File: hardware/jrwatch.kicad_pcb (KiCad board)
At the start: 4 copper layers, 36 x 36 mm, 47 parts, among them J1 TYPE-C-31-M-12, J2 FH12A-10S-0.5SH, J3 SM02B-SRSS-TB, J4 TC2030-IDC-NL, SW1 PWR/SHIP, SW2 USER, U1 MDBT50Q-1MV2, U2 nPM1300-QEAA-R7, U3 BMI270, U4 USBLC6-2SC6, Y1 32.768kHz

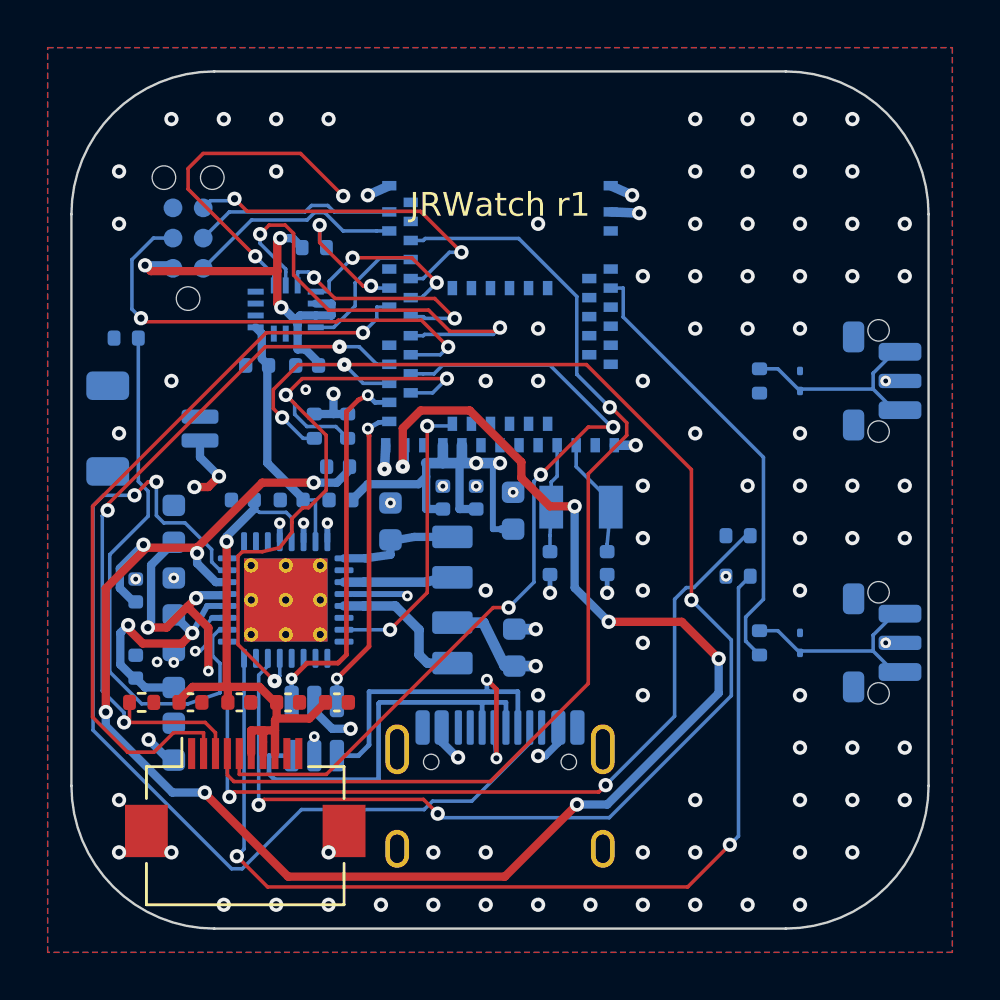
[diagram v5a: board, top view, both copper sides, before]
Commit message: WIP: land D-025 display connector rework (routing incomplete)
Scripted landing of D-025 via hardware/scripts/land_d025.py: J2 moved to
(100, 111.8) with tail-centered pads and mirrored pinout per Sharp fig 8-1,
USB CONN highways moved north, DM_CONN crossover rerouted through new vias,
CC1/CC2 landed on J1.A5/B5. Every coordinate hand clearance-checked
(0.13 mm copper, 0.25 mm hole-to-copper, 0.5 mm hole-to-hole).

State at this commit: DRC 32 errors / 20 unconnected (drc-links.json,
2026-07-03 12:57) — interactive routing cleanup still required before the
fab order gate.
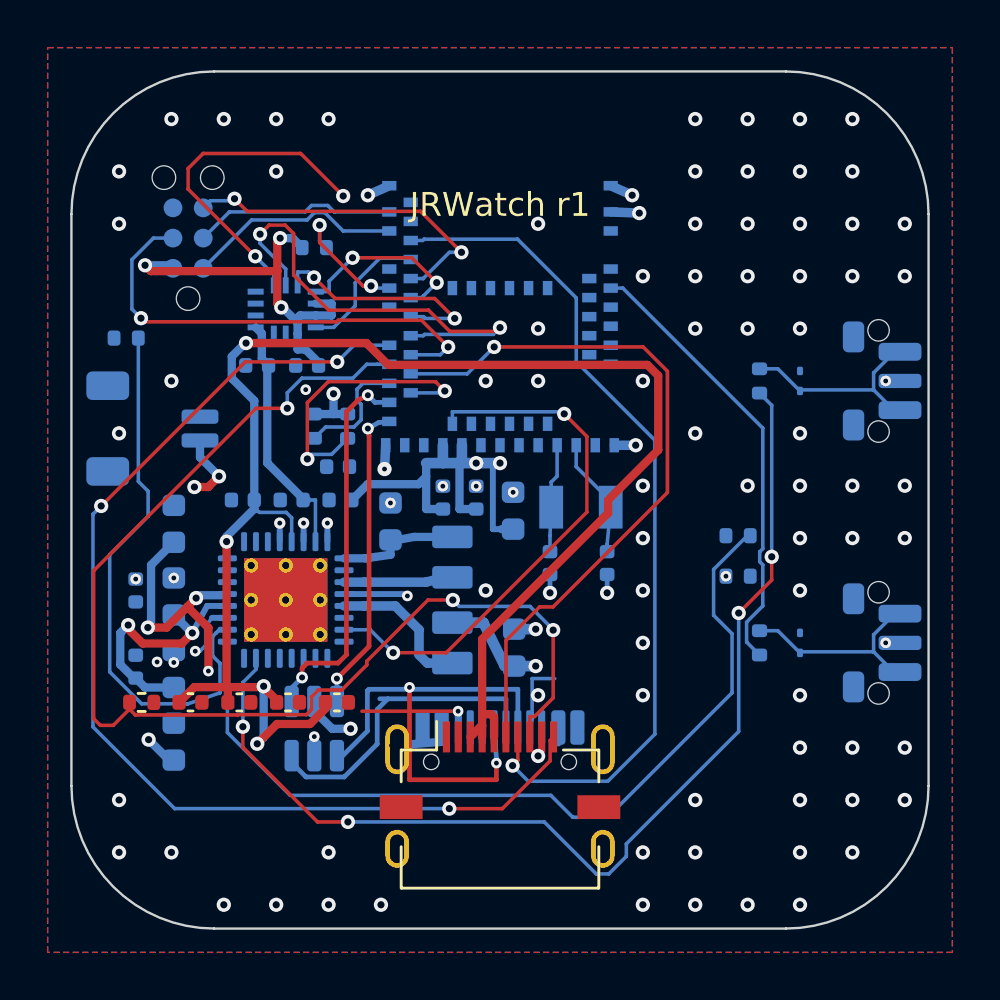
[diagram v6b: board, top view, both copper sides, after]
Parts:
- moved J2 10.7 mm to (100.0, 111.8)
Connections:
- J2 pad 1: DISP_SCK -> GND
- J2 pad 10: GND -> DISP_SCK
- J2 pad 2: DISP_MOSI -> GND
- J2 pad 3: DISP_CS -> VDD_DISP
- J2 pad 4: EXTCOMIN -> VDD_DISP
- J2 pad 5: DISP_ON -> VDD_DISP
- J2 pad 6: VDD_DISP -> DISP_ON
- J2 pad 7: VDD_DISP -> EXTCOMIN
- J2 pad 8: VDD_DISP -> DISP_CS
- J2 pad 9: GND -> DISP_MOSI
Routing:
- net VBUS_OUT: track 79.6 -> 0.00 mm, vias 10 -> 0
- net I2C_SCL: track 64.0 -> 5.10 mm, vias 5 -> 0
- net DISP_SCK: track 0.00 -> 46.8 mm, vias 0 -> 3
- net SHPHLD: track 0.00 -> 44.8 mm, vias 0 -> 4
- net VDD_DISP: track 23.9 -> 68.1 mm, vias 1 -> 4
- net N$4: track 42.0 -> 0.00 mm, vias 2 -> 0
- net CC1: track 41.8 -> 3.27 mm, vias 2 -> 1
- net DISP_MOSI: track 31.6 -> 0.00 mm, vias 1 -> 0
- net DISP_CS: track 30.2 -> 50.6 mm
- net I2C_SDA: track 29.2 -> 12.2 mm, vias 3 -> 2
- net PMIC_INT: track 12.2 -> 22.8 mm
- net EXTCOMIN: track 43.7 -> 36.1 mm
- net CC2: track 0.00 -> 4.73 mm, vias 0 -> 1
- net DISP_ON: track 34.8 -> 30.2 mm, vias 3 -> 1
- net USB_DM_CONN: track 16.8 -> 21.2 mm
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
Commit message: WIP: D-025 layout - J2 at final position (100,107.75) with mirrored nets, USB CONN re-lays, CC landings; south fabric needs interactive re-route (37 DRC items)
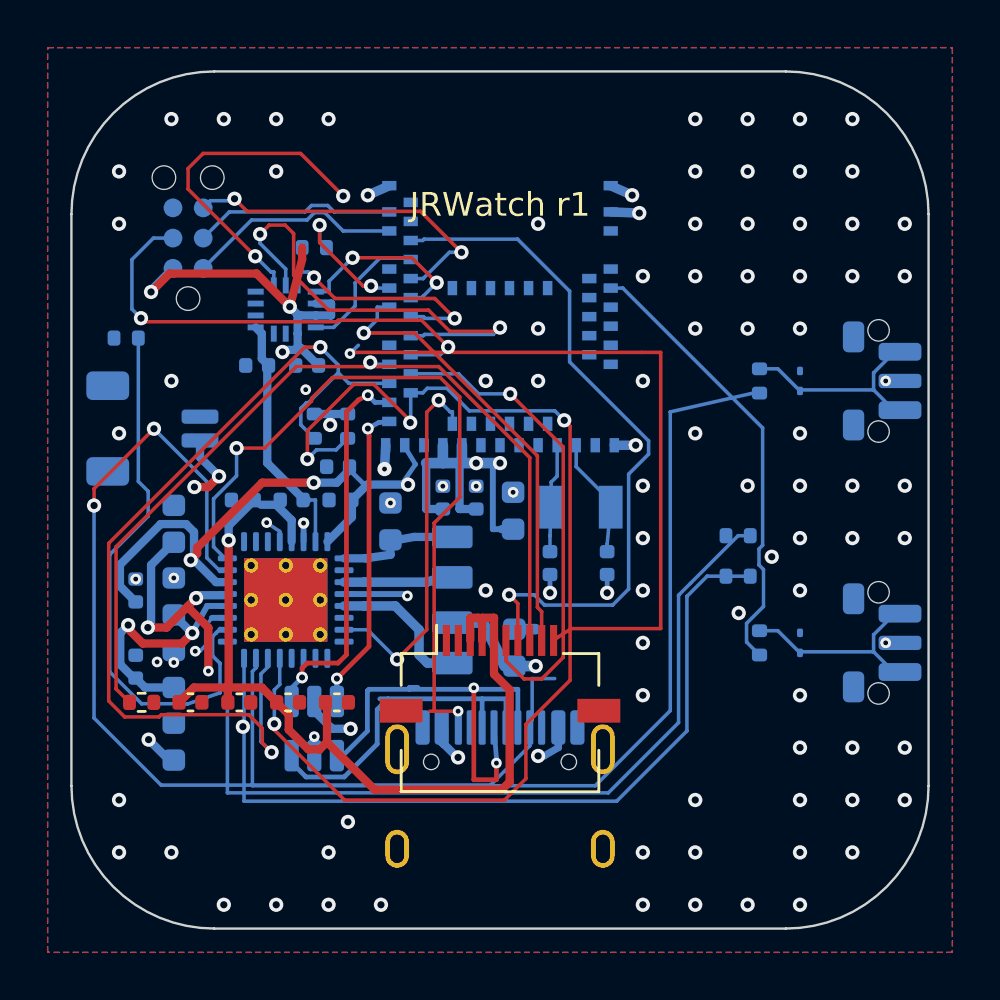
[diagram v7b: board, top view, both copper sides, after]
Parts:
- moved J2 4.05 mm to (100.0, 107.8)
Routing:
- net CC1: track 3.27 -> 44.6 mm, vias 1 -> 2
- net I2C_SDA: track 12.2 -> 48.6 mm, vias 2 -> 4
- net N$4: track 0.00 -> 34.2 mm
- net I2C_SCL: track 5.10 -> 38.7 mm, vias 0 -> 2
- net VDD_DISP: track 68.1 -> 39.9 mm, vias 4 -> 1
- net CC2: track 4.73 -> 31.9 mm, vias 1 -> 2
- net VBUS_OUT: track 0.00 -> 21.8 mm, vias 0 -> 2
- net DISP_MOSI: track 0.00 -> 19.1 mm, vias 0 -> 1
- net DISP_SCK: track 46.8 -> 29.8 mm, vias 3 -> 1
- net DISP_CS: track 50.6 -> 37.6 mm, vias 3 -> 1
- net DISP_ON: track 30.2 -> 20.5 mm
- net PMIC_INT: track 22.8 -> 15.6 mm
- net EXTCOMIN: track 36.1 -> 29.4 mm
- net SHPHLD: track 44.8 -> 40.4 mm
- net USB_DM_CONN: track 21.2 -> 18.8 mm
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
